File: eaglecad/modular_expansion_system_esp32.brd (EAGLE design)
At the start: 90.2 x 100 mm, 34 parts, among them IC1 74LS30N, IC10 74LS244N, IC2 74LS04N, IC3 74LS04N, IC4 74LS00N, IC5 74LS04N, IC6 74LS74N, IC7 74LS00N, IC9 74S373N, J1 J1_ADDRESS_CON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

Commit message: updated esp32 board
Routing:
- net D7: track 121.5 -> 120.5 mm
- net WIFI_OUT_LV_: track 37.0 -> 36.4 mm
- net D0: track 111.0 -> 110.4 mm
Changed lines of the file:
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@@
 <setting verticaltext="up"/>
 </settings>
-<grid distance="0.635" unitdist="mm" unit="mm" style="lines" multiple="1" display="no" altdistance="0.0635" altunitdist="mm" altunit="mm"/>
+<grid distance="0.3175" unitdist="mm" unit="mm" style="lines" multiple="1" display="no" altdistance="0.03175" altunitdist="mm" altunit="mm"/>
 <layers>
 <layer number="1" name="Top" color="4" fill="1" visible="yes" active="yes"/>
@@
 <wire x1="26.25" y1="51.25" x2="27.635" y2="51.25" width="0.3025" layer="16"/>
 <wire x1="24.25" y1="53.25" x2="26.25" y2="51.25" width="0.3025" layer="16"/>
-<wire x1="59.5" y1="97.75" x2="59.69" y2="97.79" width="0.3025" layer="16"/>
 <wire x1="24.25" y1="53.25" x2="24.13" y2="53.34" width="0.3025" layer="16"/>
 <wire x1="59.69" y1="97.79" x2="57.15" y2="95.25" width="0.3025" layer="16"/>
@@
 <contactref element="IC9" pad="18"/>
 <contactref element="IC10" pad="9"/>
-<wire x1="19.25" y1="2.75" x2="19.05" y2="2.54" width="0.3025" layer="16"/>
 <wire x1="75" y1="57.5" x2="75" y2="54.75" width="0.3025" layer="16"/>
 <wire x1="78.75" y1="61.25" x2="75" y2="57.5" width="0.3025" layer="16"/>
@@
 <wire x1="77.25" y1="52.5" x2="77.75" y2="52.5" width="0.3025" layer="16"/>
 <wire x1="75" y1="54.75" x2="77.25" y2="52.5" width="0.3025" layer="16"/>
-<wire x1="19.25" y1="2.75" x2="19.05" y2="2.54" width="0.3025" layer="1"/>
 <wire x1="75" y1="54.75" x2="74.93" y2="54.61" width="0.3025" layer="16"/>
 <via x="60.25" y="23.75" extent="1-16" drill="0.35"/>
@@
 <contactref element="IC9" pad="14"/>
 <contactref element="IC10" pad="5"/>
-<wire x1="24.25" y1="2.75" x2="24.13" y2="2.54" width="0.3025" layer="1"/>
 <wire x1="65" y1="57.75" x2="65" y2="56.615" width="0.3025" layer="16"/>
 <wire x1="65" y1="56.615" x2="65" y2="54.75" width="0.3025" layer="16"/>
@@
 <contactref element="IC9" pad="13"/>
 <contactref element="IC10" pad="3"/>
-<wire x1="26.5" y1="2.75" x2="26.67" y2="2.54" width="0.3025" layer="1"/>
 <wire x1="62.25" y1="56.5" x2="62.25" y2="54.75" width="0.3025" layer="16"/>
 <wire x1="63.5" y1="57.75" x2="62.25" y2="56.5" width="0.3025" layer="16"/>
@@
 <contactref element="IC9" pad="7"/>
 <contactref element="IC10" pad="16"/>
-<wire x1="31.75" y1="2.75" x2="31.75" y2="2.54" width="0.3025" layer="16"/>
 <wire x1="65" y1="70" x2="65" y2="62.25" width="0.3025" layer="16"/>
 <wire x1="68.5" y1="73.5" x2="65" y2="70" width="0.3025" layer="16"/>
@@
 <wire x1="65" y1="62.25" x2="64.77" y2="62.23" width="0.3025" layer="16"/>
 <wire x1="68.5" y1="74.25" x2="68.58" y2="74.295" width="0.3025" layer="16"/>
-<wire x1="31.75" y1="9" x2="31.75" y2="2.54" width="0.3025" layer="1"/>
-<wire x1="31.865" y1="9.115" x2="31.75" y2="9" width="0.3025" layer="1"/>
+<wire x1="31.75" y1="9" x2="31.865" y2="9.115" width="0.3025" layer="1"/>
 <wire x1="31.865" y1="12.96" x2="31.865" y2="9.115" width="0.3025" layer="1"/>
 <wire x1="31.865" y1="21.615" x2="31.865" y2="12.96" width="0.3025" layer="16"/>
@@
 <wire x1="35.5" y1="55.38833125" x2="35.5" y2="35" width="0.3025" layer="1"/>
 <wire x1="36.27913125" y1="56.13675" x2="35.84228125" y2="55.6999" width="0.3025" layer="1"/>
+<wire x1="31.75" y1="2.54" x2="31.75" y2="9" width="0.3025" layer="1"/>
 </signal>
 <signal name="D6">
@@
 <contactref element="IC9" pad="4"/>
 <contactref element="IC10" pad="14"/>
-<wire x1="34.5" y1="2.75" x2="34.29" y2="2.54" width="0.3025" layer="16"/>
 <wire x1="72.5" y1="72.75" x2="72.5" y2="62.25" width="0.3025" layer="16"/>
 <wire x1="73.5" y1="73.75" x2="72.5" y2="72.75" width="0.3025" layer="16"/>
@@
 <wire x1="72.5" y1="62.25" x2="72.39" y2="62.23" width="0.3025" layer="16"/>
 <wire x1="73.5" y1="74.25" x2="73.66" y2="74.295" width="0.3025" layer="16"/>
-<wire x1="38.5" y1="6.75" x2="34.29" y2="2.54" width="0.3025" layer="1"/>
-<wire x1="38.5" y1="15.75" x2="38.5" y2="6.75" width="0.3025" layer="1"/>
+<wire x1="38.5" y1="6.75" x2="38.5" y2="15.75" width="0.3025" layer="1"/>
 <wire x1="53.25" y1="15.75" x2="38.5" y2="15.75" width="0.3025" layer="1"/>
 <wire x1="61.25" y1="23.75" x2="53.25" y2="15.75" width="0.3025" layer="1"/>
@@
 <via x="69.75" y="41.75" extent="1-16" drill="0.35"/>
 <via x="69.25" y="59" extent="1-16" drill="0.35"/>
+<wire x1="34.29" y1="2.54" x2="38.5" y2="6.75" width="0.3025" layer="1"/>
 </signal>
 <signal name="D7">
@@
 <contactref element="IC9" pad="3"/>
 <contactref element="IC10" pad="12"/>
-<wire x1="37" y1="2.75" x2="37.5" y2="2.75" width="0.3025" layer="16"/>
-<wire x1="37" y1="2.75" x2="36.83" y2="2.54" width="0.3025" layer="16"/>
 <wire x1="77.5" y1="64.75" x2="77.25" y2="64.5" width="0.3025" layer="1"/>
 <wire x1="77.25" y1="64.5" x2="75" y2="62.25" width="0.3025" layer="1"/>
@@
 <wire x1="75" y1="62.25" x2="74.93" y2="62.23" width="0.3025" layer="1"/>
 <wire x1="78.5" y1="74.25" x2="78.74" y2="74.295" width="0.3025" layer="1"/>
-<wire x1="39" y1="4.75" x2="37" y2="2.75" width="0.3025" layer="1"/>
-<wire x1="39" y1="15" x2="39" y2="4.75" width="0.3025" layer="1"/>
-<wire x1="67.75" y1="15" x2="39" y2="15" width="0.3025" layer="1"/>
+<wire x1="37" y1="2.75" x2="39" y2="4.75" width="0.3025" layer="1"/>
+<wire x1="39" y1="14.6825" x2="39" y2="4.75" width="0.3025" layer="1"/>
+<wire x1="67.75" y1="15" x2="67.4325" y2="14.6825" width="0.3025" layer="1"/>
+<wire x1="67.4325" y1="14.6825" x2="39" y2="14.6825" width="0.3025" layer="1"/>
 <wire x1="87.75" y1="51.25" x2="82" y2="57" width="0.3025" layer="16"/>
 <wire x1="82" y1="62.75" x2="82" y2="57" width="0.3025" layer="16"/>
 <wire x1="80.25" y1="64.5" x2="82" y2="62.75" width="0.3025" layer="1"/>
 <wire x1="77.25" y1="64.5" x2="80.25" y2="64.5" width="0.3025" layer="1"/>
-<wire x1="37" y1="2.75" x2="36.83" y2="2.54" width="0.3025" layer="1"/>
 <via x="67.75" y="15" extent="1-16" drill="0.35"/>
 <via x="82" y="62.75" extent="1-16" drill="0.35"/>
@@
 <wire x1="68.34" y1="15" x2="87.75" y2="34.41" width="0.3025" layer="16"/>
 <wire x1="87.75" y1="34.41" x2="87.75" y2="51.25" width="0.3025" layer="16"/>
+<wire x1="36.83" y1="2.54" x2="37" y2="2.71" width="0.3025" layer="1"/>
+<wire x1="37" y1="2.71" x2="37" y2="2.75" width="0.3025" layer="1"/>
 </signal>
 <signal name="RAS*">
@@
 <wire x1="10" y1="52.5" x2="11.25" y2="51.25" width="0.3025" layer="16"/>
 <wire x1="13.75" y1="64.75" x2="13.97" y2="64.77" width="0.3025" layer="16"/>
-<wire x1="16.5" y1="53.5" x2="16.51" y2="53.34" width="0.3025" layer="16"/>
 <wire x1="10.665" y1="59.56" x2="11.56" y2="59.56" width="0.3025" layer="16"/>
 <wire x1="10" y1="52.5" x2="10" y2="58.895" width="0.3025" layer="16"/>
@@
 <contactref element="U1" pad="8"/>
 <contactref element="B1" pad="LV3"/>
-<wire x1="60.25" y1="13.25" x2="58.5" y2="11.5" width="0.3025" layer="1"/>
-<wire x1="65" y1="13.25" x2="60.25" y2="13.25" width="0.3025" layer="1"/>
-<wire x1="82.5" y1="30.75" x2="65" y2="13.25" width="0.3025" layer="16"/>
+<wire x1="59.615" y1="12.615" x2="58.5" y2="11.5" width="0.3025" layer="1"/>
+<wire x1="64.365" y1="12.615" x2="59.615" y2="12.615" width="0.3025" layer="1"/>
+<wire x1="82.5" y1="30.75" x2="64.365" y2="12.615" width="0.3025" layer="16"/>
 <wire x1="82.5" y1="40.5" x2="82.5" y2="30.75" width="0.3025" layer="16"/>
 <wire x1="58.5" y1="11.5" x2="58.345" y2="11.43" width="0.3025" layer="1"/>
 <wire x1="82.5" y1="40.5" x2="82.55" y2="40.64" width="0.3025" layer="16"/>
-<via x="65" y="13.25" extent="1-16" drill="0.35"/>
+<via x="64.365" y="12.615" extent="1-16" drill="0.35"/>
 </signal>
 <signal name="D5_LV">
@@
 <contactref element="U1" pad="11"/>
 <contactref element="B2" pad="LV4"/>
-<wire x1="50.75" y1="14.25" x2="65.75" y2="14.25" width="0.3025" layer="1"/>
-<wire x1="50.75" y1="24.25" x2="50.75" y2="14.25" width="0.3025" layer="16"/>
+<wire x1="66.395" y1="13.615" x2="50.75" y2="13.615" width="0.3025" layer="1"/>
+<wire x1="50.75" y1="24.25" x2="50.75" y2="13.615" width="0.3025" layer="16"/>
 <wire x1="38.25" y1="36.75" x2="50.75" y2="24.25" width="0.3025" layer="16"/>
 <wire x1="38.25" y1="41.25" x2="38.25" y2="36.75" width="0.3025" layer="1"/>
 <wire x1="38.25" y1="41.25" x2="38.1" y2="41.275" width="0.3025" layer="1"/>
-<via x="50.75" y="14.25" extent="1-16" drill="0.35"/>
+<via x="50.75" y="13.615" extent="1-16" drill="0.35"/>
 <via x="38.25" y="36.75" extent="1-16" drill="0.35"/>
-<wire x1="65.75" y1="14.25" x2="65.76" y2="14.25" width="0.3025" layer="1"/>
 <wire x1="66.675" y1="13.335" x2="66.675" y2="12.14" width="0.3025" layer="1"/>
 <wire x1="66.675" y1="12.14" x2="65.965" y2="11.43" width="0.3025" layer="1"/>
-<wire x1="65.76" y1="14.25" x2="66.675" y2="13.335" width="0.3025" layer="1"/>
+<wire x1="66.395" y1="13.615" x2="66.675" y2="13.335" width="0.3025" layer="1"/>
 </signal>
 <signal name="D2_LV">
@@
 <wire x1="50.5" y1="11.5" x2="50.725" y2="11.43" width="0.3025" layer="16"/>
 <via x="53.25" y="34.385" extent="1-16" drill="0.35"/>
-<wire x1="57.785" y1="40.64" x2="57.785" y2="40.005" width="0.3025" layer="1"/>
 <wire x1="59.42865" y1="37.27886875" x2="59.42865" y2="36.38113125" width="0.3025" layer="1"/>
 <wire x1="59.42865" y1="36.38113125" x2="57.66251875" y2="34.615" width="0.3025" layer="1"/>
 <wire x1="57.66251875" y1="34.615" x2="53.48" y2="34.615" width="0.3025" layer="1"/>
-<wire x1="57.785" y1="40.64" x2="57.785" y2="38.92251875" width="0.3025" layer="1"/>
-<wire x1="57.785" y1="38.92251875" x2="59.42865" y2="37.27886875" width="0.3025" layer="1"/>
+<wire x1="59.42865" y1="37.27886875" x2="57.785" y2="38.92251875" width="0.3025" layer="1"/>
+<wire x1="57.785" y1="38.92251875" x2="57.785" y2="40.64" width="0.3025" layer="1"/>
 </signal>
 <signal name="WIFI_IN">

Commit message: added power supply stuff
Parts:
- moved C7 7.31 mm to (75.9, 97.5)
- moved IC6 7.31 mm to (75.9, 86.0)
- moved J3-WAIT 7.31 mm to (66.7, 88.9)
- moved RGBLED2 7.31 mm to (68.9, 4.76)
- moved B2 7.31 mm to (35.9, 47.9)
- moved B3 7.31 mm to (49.8, 85.4)
- moved B4 7.31 mm to (54.3, 46.0)
- moved B5 7.31 mm to (14.9, 14.3)
- moved C1 7.31 mm to (23.2, 38.4)
- moved C2 7.31 mm to (23.2, 49.8)
- moved C3 7.31 mm to (23.2, 61.3)
- moved C4 7.31 mm to (35.2, 59.4)
- moved C5 7.31 mm to (23.2, 72.7)
- moved C6 7.31 mm to (23.2, 27.0)
- moved C8 7.31 mm to (47.3, 70.8)
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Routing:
- net D1_HV: track 49.8 -> 46.8 mm
- net D2_HV: track 52.2 -> 50.0 mm
- net WIFI_OUT: track 123.1 -> 125.0 mm
- net D2: track 104.1 -> 105.8 mm
- net VCC/2: track 177.9 -> 179.1 mm
- net WIFI_OUT_LV_: track 36.4 -> 37.3 mm
- net D2_LV: track 61.8 -> 62.7 mm
- net D3: track 99.8 -> 99.0 mm
- net N$3: track 51.6 -> 52.3 mm
- net D5: track 104.8 -> 105.5 mm
- net D3_LV: track 51.2 -> 51.8 mm
- net A4: track 28.8 -> 29.4 mm
- net D1_LV: track 65.9 -> 66.4 mm
- net D4: track 106.6 -> 106.1 mm
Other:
- board size 90.2 x 100 mm -> 82.8 x 100 mm

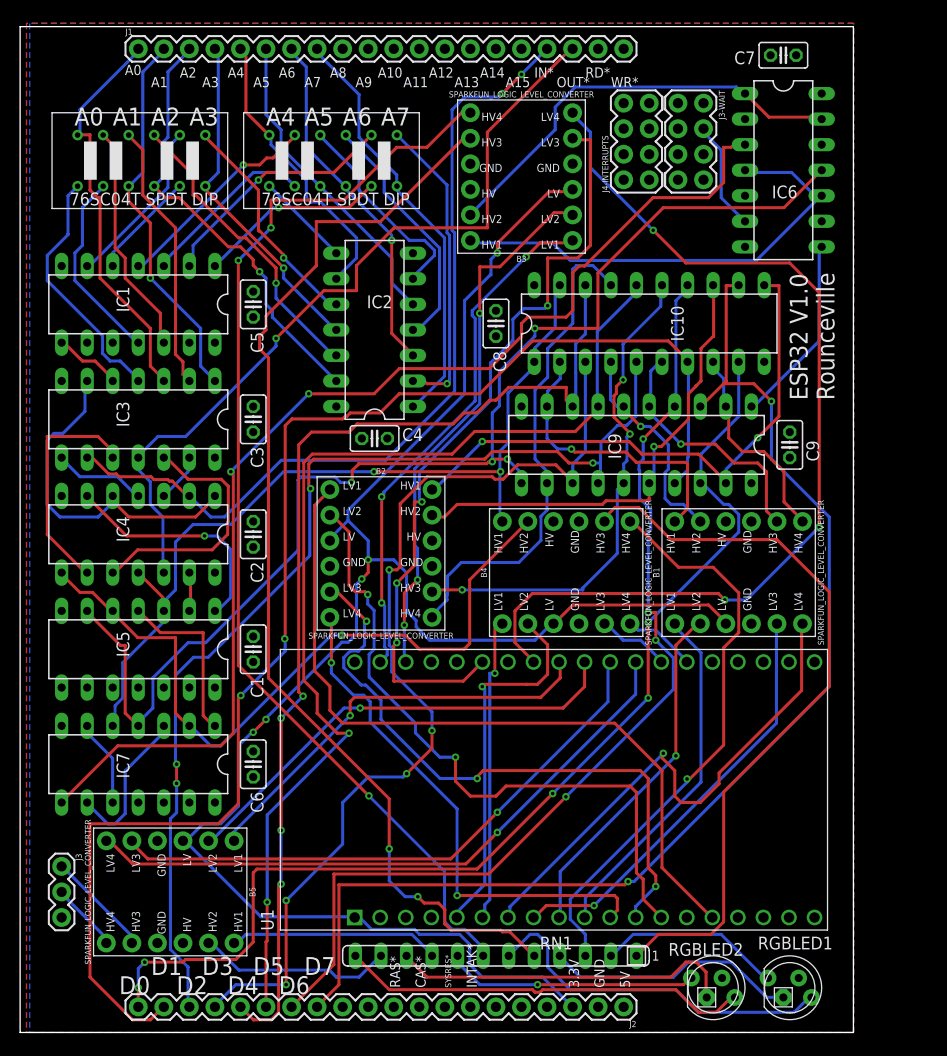
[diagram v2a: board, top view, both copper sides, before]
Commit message: first 'working' ESP32 code and board design
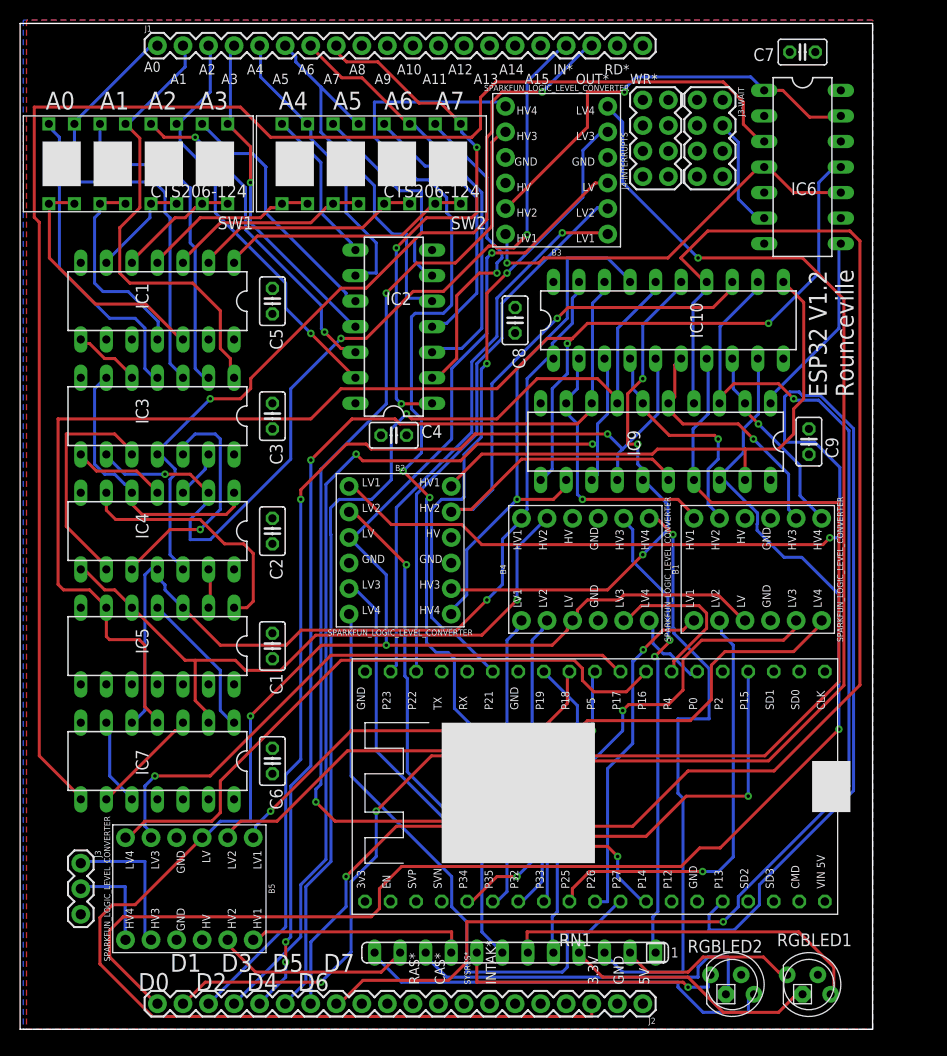
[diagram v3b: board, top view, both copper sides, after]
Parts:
- removed U1: ESP32-DEVKITC-32D, ESP32-DEVKITC-32D:MODULE_ESP32-DEVKITC-32D
- added U$1: ESP32S, TMS99:ESP32S
- SW1, SW2: value 76SC04T -> CTS206-124; device TMS99:76SC04T -> TMS99:CTS206-124
- moved SW2 25.7 mm to (46.4, 91.4)
- moved SW1 16.5 mm to (23.2, 91.4)
- moved B3 3.55 mm to (53.3, 86.0)
- moved C5 1.93 mm to (25.1, 73.0)
- moved C7 1.93 mm to (77.8, 97.8)
- moved C8 1.93 mm to (49.2, 71.1)
- moved IC10 1.93 mm to (64.5, 71.1)
- moved B5 1.93 mm to (16.8, 14.6)
- moved C1 1.93 mm to (25.1, 38.7)
- moved C2 1.93 mm to (25.1, 50.2)
- moved C9 1.93 mm to (78.4, 59.1)
- moved RN1 1.93 mm to (49.2, 8.26)
- moved C6 1.93 mm to (25.1, 27.3)
- moved IC1 1.93 mm to (13.7, 73.0)
- moved J2 1.93 mm to (61.9, 3.17)
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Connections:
- net N$17 renamed IC6_PRE_HV
- net N$18 renamed IC6_CLR_HV
- net N$27 renamed RGBLED1_B_5V
- net N$28 renamed RGBLED1_G_5V
- net N$29 renamed RGBLED1_R_5V
- net N$30 renamed RGBLED2_B_5V
- net N$31 renamed RGBLED2_G_5V
- net N$32 renamed RGBLED1_B
- net N$33 renamed RGBLED2_R_5V
- net N$34 renamed RGBLED1_G
- net N$35 renamed RGBLED1_R
- net N$36 renamed RGBLED2_B
- net N$37 renamed RGBLED2_G
- net N$38 renamed RGBLED2_R
- removed net EXT_5V: U1.19
- removed net N$1: IC1.1, SW1.IN1
- removed net N$10: B3.LV2, U1.22
- removed net N$11: B3.LV3, U1.25
- removed net N$16: B3.LV4, U1.27
- removed net N$19: B5.LV1, U1.28
- removed net N$2: IC1.2, SW1.IN2
- removed net N$22: B5.LV2, U1.29
- removed net N$25: B4.LV3, U1.32
- removed net N$26: B4.LV4, U1.33
- removed net N$3: B3.LV1, U1.21
- removed net N$4: IC1.3, SW1.IN3
- removed net N$5: IC1.4, SW1.IN4
- removed net N$6: IC1.5, SW2.IN1
- removed net N$7: IC1.6, SW2.IN2
- removed net N$8: IC1.11, SW2.IN3
- removed net N$9: IC1.12, SW2.IN4
- new net A0_OR_NOT_A0: IC1.12, SW1.SW4-OUT1, SW1.SW4-OUT2
- new net A1_OR_NOT_A1: IC1.11, SW1.SW3-OUT1, SW1.SW3-OUT2
- new net A2_OR_NOT_A2: IC1.6, SW1.SW2-OUT1, SW1.SW2-OUT2
- new net A3_OR_NOT_A3: IC1.5, SW1.SW1-OUT1, SW1.SW1-OUT2
- new net A4_OR_NOT_A4: IC1.4, SW2.SW4-OUT1, SW2.SW4-OUT2
- new net A5_OR_NOT_A5: IC1.3, SW2.SW3-OUT1, SW2.SW3-OUT2
- new net A6_OR_NOT_A6: IC1.2, SW2.SW2-OUT1, SW2.SW2-OUT2
- new net A7_OR_NOT_A7: IC1.1, SW2.SW1-OUT1, SW2.SW1-OUT2
- new net IC6A_CLR_LV: B3.LV2, U$1.P$36
- new net IC6A_PRE_LV: B3.LV1, U$1.P$37
- new net RGBLED1_B_LV: B4.LV3, U$1.P$26
- new net RGBLED1_G_LV: B4.LV4, U$1.P$25
- new net RGBLED1_R_LV: B3.LV3, U$1.P$33
- new net RGBLED2_B_LV: B3.LV4, U$1.P$31
- new net RGBLED2_G_LV: B5.LV1, U$1.P$30
- new net RGBLED2_R_LV: B5.LV2, U$1.P$29
- net A0: now also SW1.SW4-IN1; no longer SW2.OUTA4
- net A1: now also SW1.SW3-IN1; no longer SW2.OUT3B
- net A2: now also SW1.SW2-IN1; no longer SW2.OUT2B
- net A3: now also SW1.SW1-IN1; no longer SW2.OUT1B
- net A4: now also SW2.SW4-IN1; no longer SW1.OUTA4
- net A5: now also SW2.SW3-IN1; no longer SW1.OUT3B
- net A6: now also SW2.SW2-IN1; no longer SW1.OUT2B
- net A7: now also SW2.SW1-IN1; no longer SW1.OUT1B
- net D0_LV: now also U$1.P$15; no longer U1.15
- net D1_LV: now also U$1.P$23; no longer U1.13
- net D2_LV: now also U$1.P$12; no longer U1.12
- net D3_LV: now also U$1.P$11; no longer U1.11
- net D4_LV: now also U$1.P$10; no longer U1.10
- net D5_LV: now also U$1.P$9; no longer U1.9
- net D6_LV: now also U$1.P$8; no longer U1.8
- net D7_LV: now also U$1.P$7; no longer U1.7
- net GND: now also U$1.P$14, U$1.P$32, U$1.P$38; no longer U1.14, U1.20, U1.26
- net N$23: now also U$1.P$28; no longer U1.30
- net N$24: now also U$1.P$27; no longer U1.31
- net NOT_A0: now also SW1.SW4-IN2; no longer SW2.OUT4B
- net NOT_A1: now also SW1.SW3-IN2; no longer SW2.OUT3A
- net NOT_A2: now also SW1.SW2-IN2; no longer SW2.OUT2A
- net NOT_A3: now also SW1.SW1-IN2; no longer SW2.OUT1A
- net NOT_A4: now also SW2.SW4-IN2; no longer SW1.OUT4B
- net NOT_A5: now also SW2.SW3-IN2; no longer SW1.OUT3A
- net NOT_A6: now also SW2.SW2-IN2; no longer SW1.OUT2A
- net NOT_A7: now also SW2.SW1-IN2; no longer SW1.OUT1A
- net VCC: now also U$1.P$19
- net VCC/2: no longer U1.1
- net WIFI_IN_LV_: now also U$1.P$6; no longer U1.6
- net WIFI_OUT_LV_: now also U$1.P$5; no longer U1.5
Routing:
- net RGBLED2_B_LV: track 0.00 -> 114.2 mm, vias 0 -> 2
- net N$16: track 97.5 -> 0.00 mm, vias 3 -> 0
- net N$11: track 77.1 -> 0.00 mm, vias 4 -> 0
- net RGBLED1_R_LV: track 0.00 -> 65.4 mm, vias 0 -> 2
- net D0_LV: track 75.4 -> 138.8 mm, vias 0 -> 1
- net IC6A_PRE_LV: track 0.00 -> 55.4 mm, vias 0 -> 1
- net IC6A_CLR_LV: track 0.00 -> 54.8 mm
- net N$10: track 54.2 -> 0.00 mm, vias 3 -> 0
- net N$3: track 52.3 -> 0.00 mm, vias 3 -> 0
- net D6: track 100.6 -> 152.9 mm, vias 4 -> 1
- net RGBLED2_R_LV: track 0.00 -> 47.1 mm, vias 0 -> 1
- net N$22: track 46.2 -> 0.00 mm, vias 1 -> 0
- net N$19: track 42.3 -> 0.00 mm, vias 1 -> 0
- net RGBLED2_G_LV: track 0.00 -> 40.6 mm, vias 0 -> 1
- net WIFI_IN_OR_OUT: track 115.8 -> 152.4 mm, vias 2 -> 0
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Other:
- board size 82.8 x 100 mm -> 84.8 x 100 mm
- board text added: "ESP32 V1.2 Rounceville"
- board text removed: "ESP32 V1.0 Rounceville"
